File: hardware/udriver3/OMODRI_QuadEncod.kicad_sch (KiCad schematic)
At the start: 22 parts, among them J5 Conn_01x05, J6 Conn_01x05, U17 LSF0204RUT, U7 LSF0204RUT

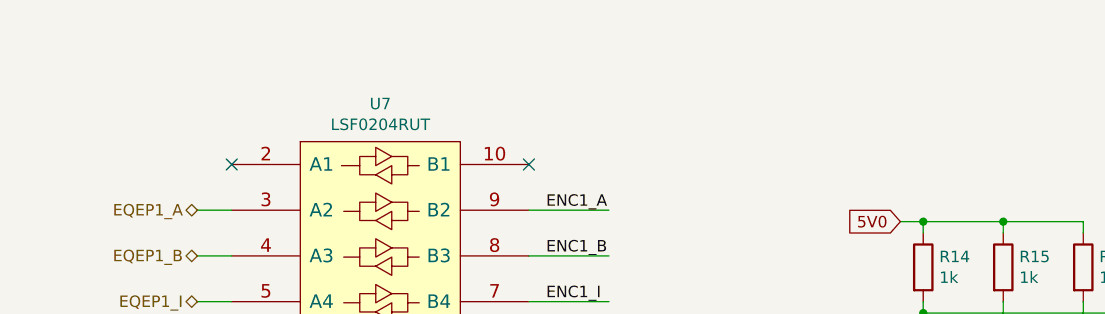
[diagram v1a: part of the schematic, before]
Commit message: Continue routing, split VM an Vpower to improve efficiency with external DC/DC buck converter
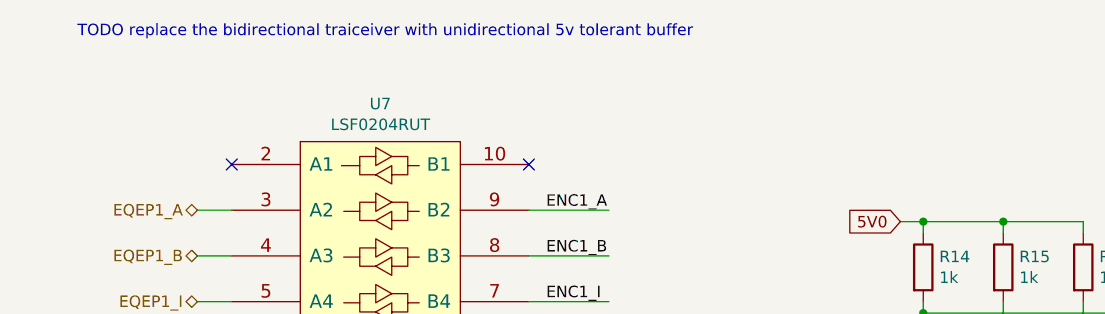
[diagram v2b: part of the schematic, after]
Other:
- note added: "TODO replace the bidirectional traiceiver with unidirectional 5v tolerant buffer"
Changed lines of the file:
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@@
     (stroke (width 0) (type default) (color 0 0 0 0))
+  )
+  (text "TODO replace the bidirectional traiceiver with unidirectional 5v tolerant buffer\n"
+    (at 90.17 29.21 0)
+    (effects (font (size 1.27 1.27)) (justify left bottom))
   )
   (label "ENC2_I" (at 210.82 102.87 0)

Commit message: Change encoder footprint for SMD DF13, continue to route DRVs
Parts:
- J5, J6: footprint udriver3:Hirose_DF13-05P-1.25DSA_1x05_P1.25mm_Vertical -> Connector_Hirose:Hirose_DF13C_CL535-0405-0-51_1x05-1MP_P1.25mm_Vertical
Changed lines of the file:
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@@
       (effects (font (size 1.27 1.27)) (justify left))
     )
-    (property "Footprint" "udriver3:Hirose_DF13-05P-1.25DSA_1x05_P1.25mm_Vertical" (id 2) (at 224.79 64.77 0)
+    (property "Footprint" "Connector_Hirose:Hirose_DF13C_CL535-0405-0-51_1x05-1MP_P1.25mm_Vertical" (id 2) (at 224.79 64.77 0)
       (effects (font (size 1.27 1.27)) hide)
     )
@@
       (effects (font (size 1.27 1.27)) (justify left))
     )
-    (property "Footprint" "udriver3:Hirose_DF13-05P-1.25DSA_1x05_P1.25mm_Vertical" (id 2) (at 224.79 102.87 0)
+    (property "Footprint" "Connector_Hirose:Hirose_DF13C_CL535-0405-0-51_1x05-1MP_P1.25mm_Vertical" (id 2) (at 224.79 102.87 0)
       (effects (font (size 1.27 1.27)) hide)
     )

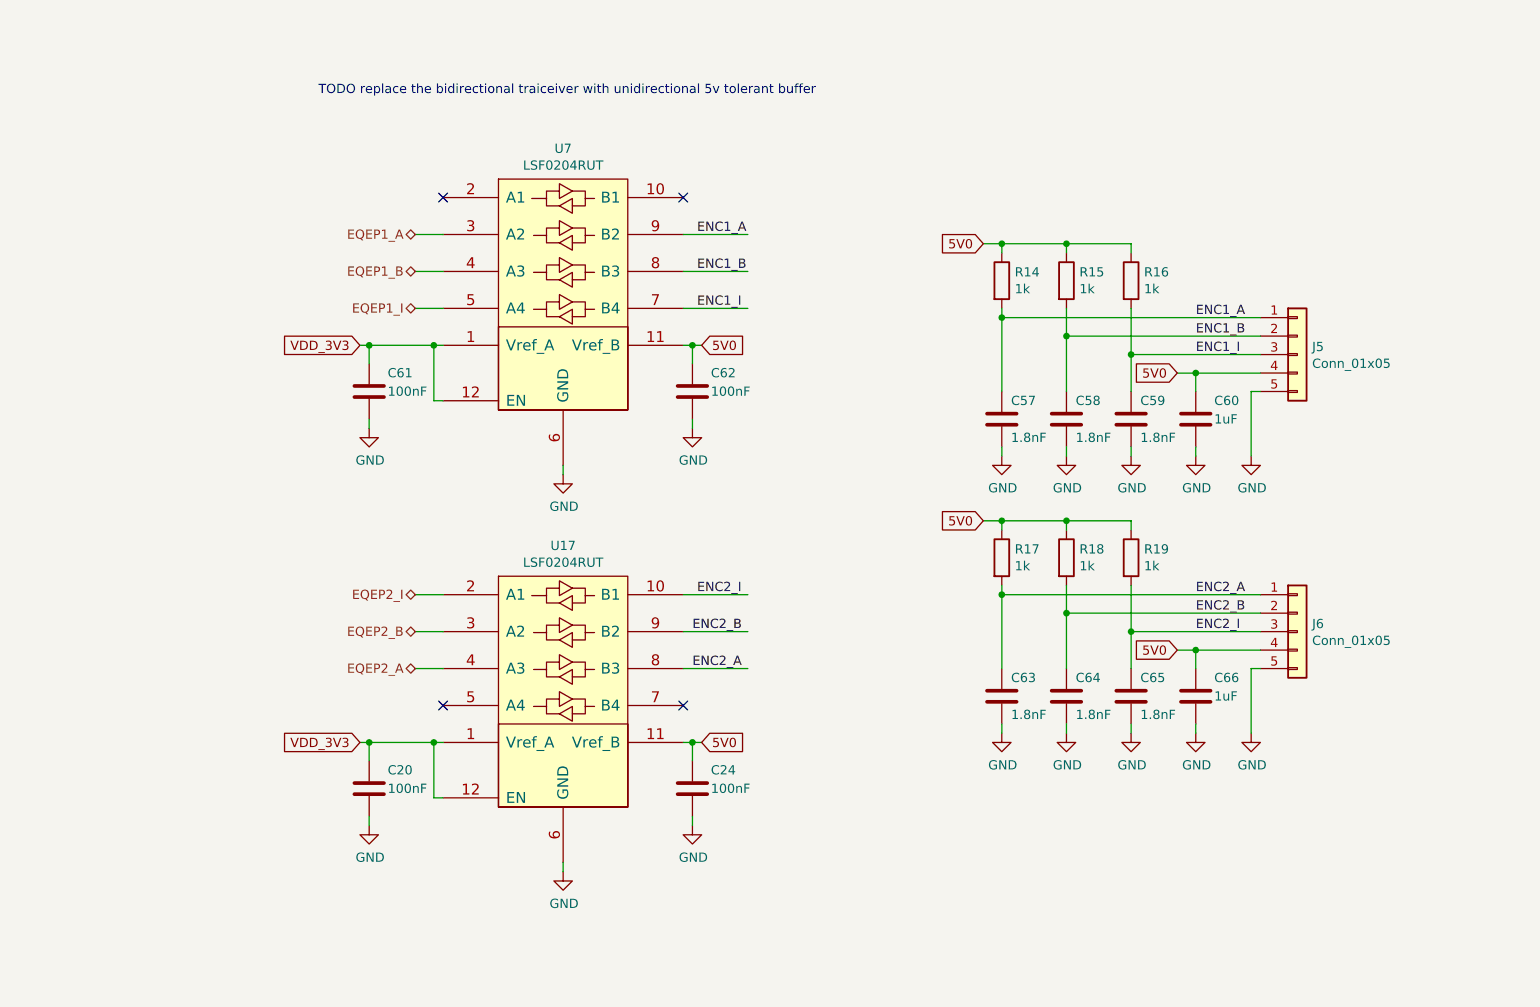
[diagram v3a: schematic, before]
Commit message: Move CAN connector, Include add DC DC back for 1.2 and 3.3V, wire the encoder, ...
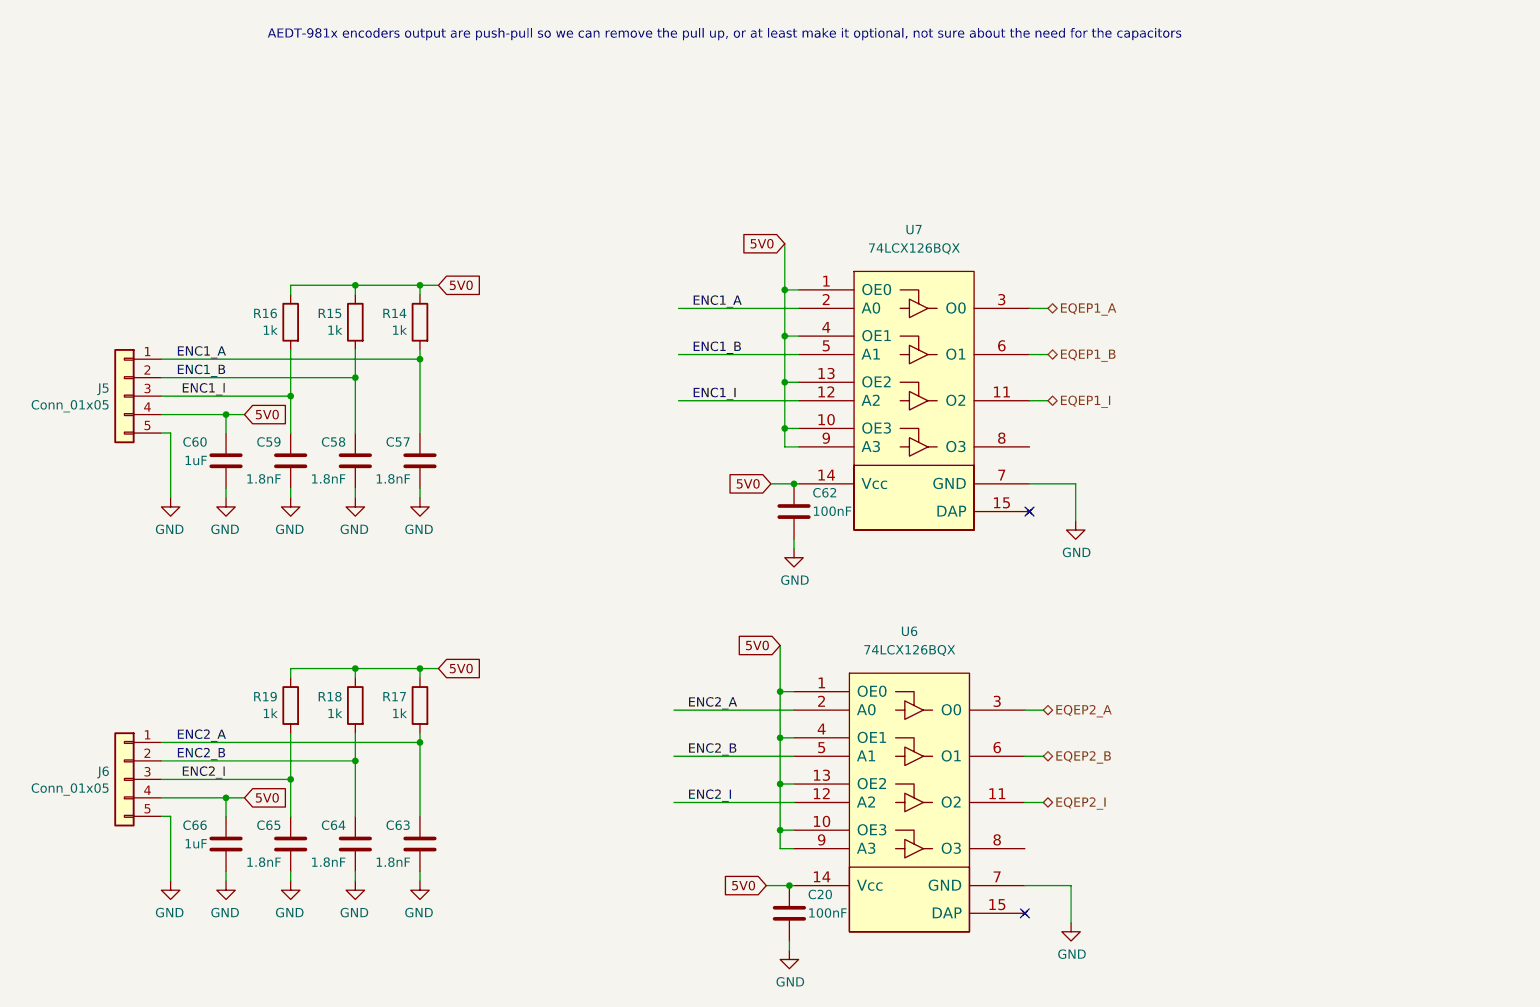
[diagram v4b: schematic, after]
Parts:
- removed C24, C61: 100nF, Capacitor_SMD:C_0201_0603Metric, symbol Device:C
- removed U17, U7: LSF0204RUT, Package_DFN_QFN:Texas_R_PUQFN-N12, symbol omodri_lib:LSF0204RUT
- added U6, U7: 74LCX126BQX, udriver3:DFN-14-1EP_3.0x2.5mm_P0.5mm_EP1.4x1.0mm, symbol omodri_lib:74LCX126BQX
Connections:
- net VDD_3V3 is gone; now on net 5V0: C20.1
- net 5V0: now also U6.1 (OE0), U6.10 (OE3), U6.13 (OE2), U6.14 (Vcc), U6.4 (OE1), U6.9 (A3), U7.1 (OE0), U7.10 (OE3), U7.13 (OE2), U7.14 (Vcc), U7.4 (OE1), U7.9 (A3)
- net ENC1_A: now also U7.2 (A0)
- net ENC1_B: now also U7.5 (A1)
- net ENC1_I: now also U7.12 (A2)
- net ENC2_A: now also U6.2 (A0)
- net ENC2_B: now also U6.5 (A1)
- net ENC2_I: now also U6.12 (A2)
- net EQEP1_A: now also U7.3 (O0)
- net EQEP1_B: now also U7.6 (O1)
- net EQEP1_I: now also U7.11 (O2)
- net EQEP2_A: now also U6.3 (O0)
- net EQEP2_B: now also U6.6 (O1)
- net EQEP2_I: now also U6.11 (O2)
- net GND: now also U6.7 (GND), U7.7 (GND)
- no-connect marks 4 -> 2
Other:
- note added: "AEDT-981x encoders output are push-pull so we can remove the pull up, or at least make it optional, not sure about the need for the capacitors"
- note removed: "TODO replace the bidirectional traiceiver with unidirectional 5v tolerant buffer"
- moved on the sheet: C20, C57, C58, C59, C60, C62, C63, C64, C65, C66, J5, J6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

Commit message: Use angle DF13 connector for SPI, CAN and encoders, add 3d step files, route
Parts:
- J5, J6: footprint Connector_Hirose:Hirose_DF13C_CL535-0405-0-51_1x05-1MP_P1.25mm_Vertical -> udriver3:DF135P125H76
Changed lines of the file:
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@@
       (effects (font (size 1.27 1.27)) (justify left))
     )
-    (property "Footprint" "Connector_Hirose:Hirose_DF13C_CL535-0405-0-51_1x05-1MP_P1.25mm_Vertical" (id 2) (at 63.5 70.485 0)
+    (property "Footprint" "udriver3:DF135P125H76" (id 2) (at 63.5 70.485 0)
       (effects (font (size 1.27 1.27)) hide)
     )
@@
       (effects (font (size 1.27 1.27)) (justify left))
     )
-    (property "Footprint" "Connector_Hirose:Hirose_DF13C_CL535-0405-0-51_1x05-1MP_P1.25mm_Vertical" (id 2) (at 63.5 123.19 0)
+    (property "Footprint" "udriver3:DF135P125H76" (id 2) (at 63.5 123.19 0)
       (effects (font (size 1.27 1.27)) hide)
     )

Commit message: Schematics update. 12V0 and 5V0 power supplies not finished yet. RS485 added but not connected to F28388 mcu.
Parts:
- C20, C62: Rated Voltage 10V -> 25V
- C57, C58, C59, C63, C64, C65: Rated Voltage 50V -> 25V
- U6, U7: DigiKey (none) -> 74LCX126BQXTR-ND; Farnell (none) -> 3368284; Mouser (none) -> 512-74LCX126BQX; Part No (none) -> 74LCX126BQX
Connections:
- no-connect marks 2 -> 4
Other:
- moved on the sheet: C20, C62, U6, U7

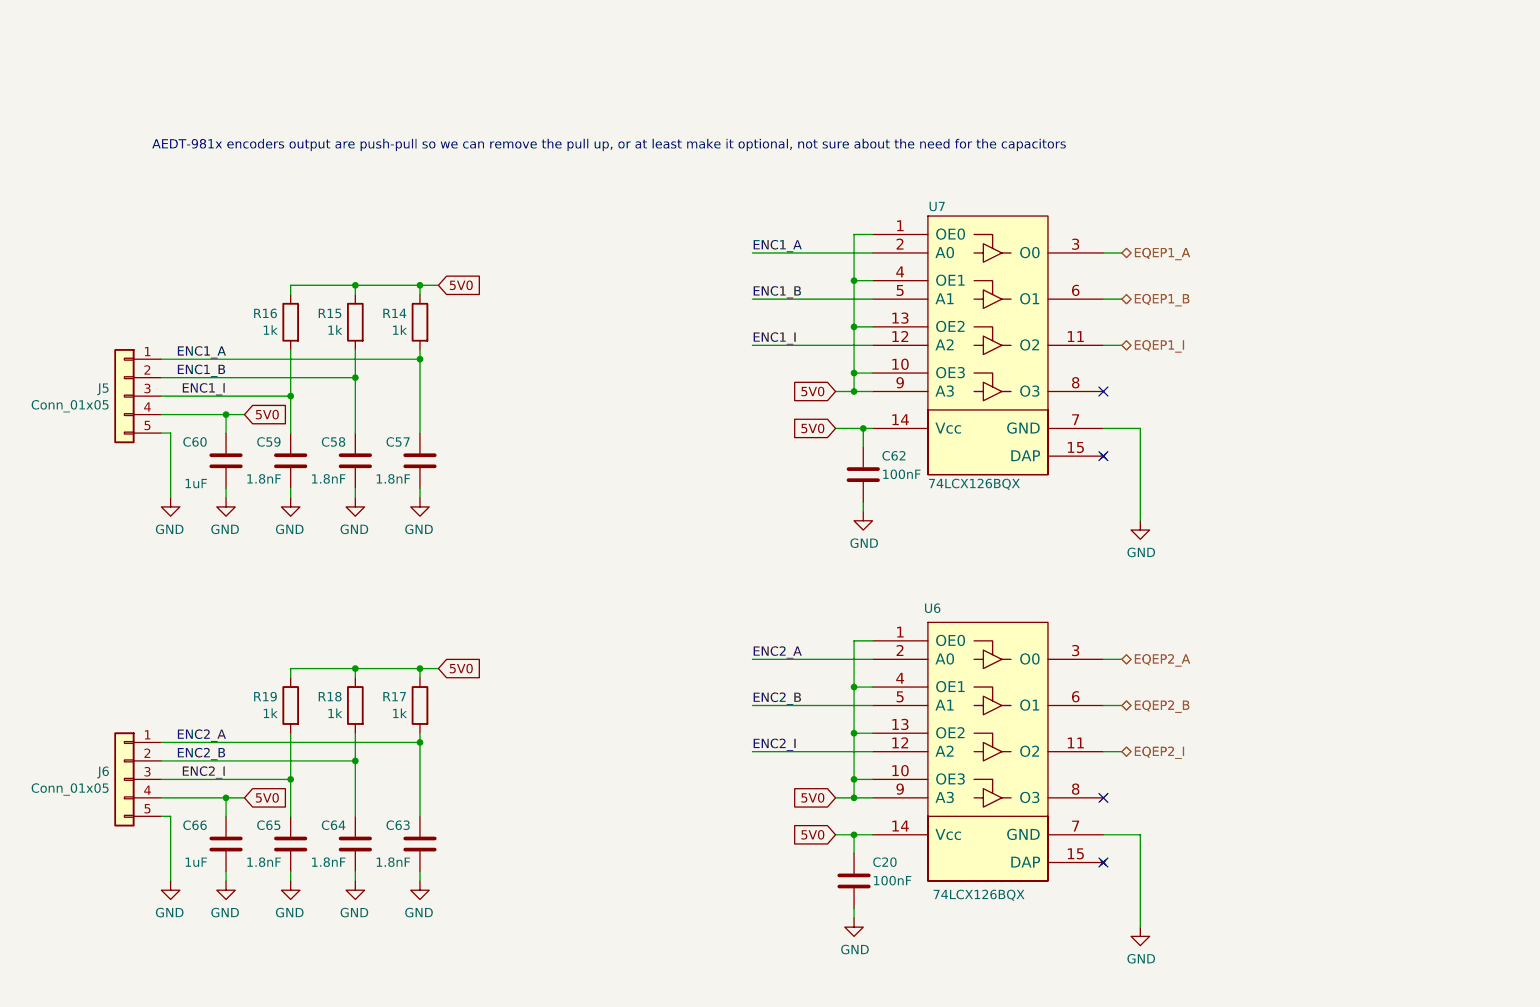
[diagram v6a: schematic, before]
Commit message: Temporary version of udrive3 v2.0. - In schematic there are 2 solutions for DC/DC buck converter. - PCB routing is not finished yet.
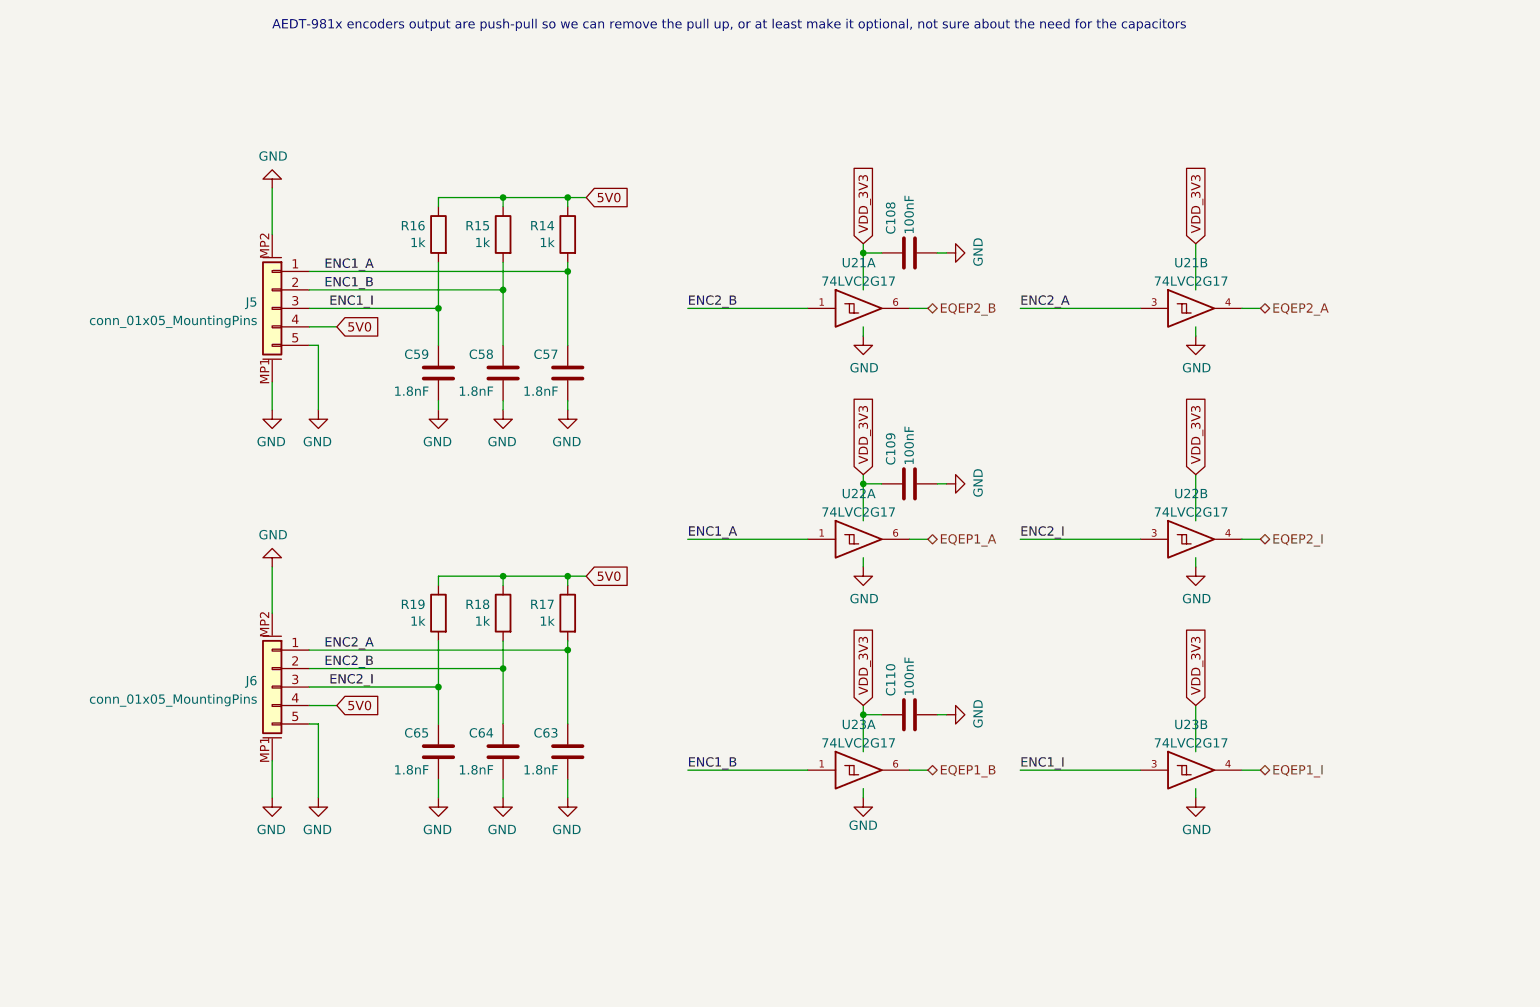
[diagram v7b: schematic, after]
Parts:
- removed C20, C62: 100nF, Capacitor_SMD:C_0201_0603Metric, symbol Device:C
- removed C60, C66: 1uF, Capacitor_SMD:C_0201_0603Metric, symbol Device:C
- removed J5, J6: Conn_01x05, udriver3:DF135P125H76, symbol Connector_Generic:Conn_01x05
- removed U6, U7: 74LCX126BQX, udriver3:DFN-14-1EP_3.0x2.5mm_P0.5mm_EP1.4x1.0mm, symbol omodri_lib:74LCX126BQX
- added C108, C109, C110: 100nF, Capacitor_SMD:C_0201_0603Metric, symbol Device:C
- added J5, J6: conn_01x05_MountingPins, udriver3:Hirose_DF13_05P-1.25H_1x05_P1.25mm_Right_angle, symbol omodri_lib:conn_01x05_MountingPins
- added U21, U22, U23: 74LVC2G17, udriver3:USON-6_1.45x1.0mm_P0.5mm, symbol 74xGxx:74LVC2G17
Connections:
- net 5V0: now also J5.4 (Pin_4), J6.4 (Pin_4)
- net ENC1_A: now also J5.1 (Pin_1), U22.1
- net ENC1_B: now also J5.2 (Pin_2), U23.1
- net ENC1_I: now also J5.3 (Pin_3), U23.3
- net ENC2_A: now also J6.1 (Pin_1), U21.3
- net ENC2_B: now also J6.2 (Pin_2), U21.1
- net ENC2_I: now also J6.3 (Pin_3), U22.3
- net EQEP1_A: now also U22.6
- net EQEP1_B: now also U23.6
- net EQEP1_I: now also U23.4
- net EQEP2_A: now also U21.4
- net EQEP2_B: now also U21.6
- net EQEP2_I: now also U22.4
- net GND: now also C108.2, C109.2, C110.2, J5.5 (Pin_5), J5.MP1 (MountPin1), J5.MP2 (MountPin2), J6.5 (Pin_5), J6.MP1 (MountPin1), J6.MP2 (MountPin2), U21.2 (GND), U21.2 (GND), U22.2 (GND), U22.2 (GND), U23.2 (GND), U23.2 (GND)
- new net VCC: C108.1, C109.1, C110.1, U21.5 (VCC), U21.5 (VCC), U22.5 (VCC), U22.5 (VCC), U23.5 (VCC), U23.5 (VCC)
- no-connect marks 4 -> 0
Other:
- moved on the sheet: C57, C58, C59, C63, C64, C65, R14, R15, R16, R17, R18, R19
